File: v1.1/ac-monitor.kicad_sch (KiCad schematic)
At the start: 5 parts, among them U7 MID400

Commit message: cleanups all over
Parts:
- C10: renamed from C7; footprint Capacitor_SMD:C_0603_1608Metric_Pad1.05x0.95mm_HandSolder -> Capacitor_SMD:C_0603_1608Metric_Pad1.08x0.95mm_HandSolder
- R16: renamed from R29; footprint Resistor_SMD:R_1206_3216Metric_Pad1.42x1.75mm_HandSolder -> Resistor_SMD:R_1206_3216Metric_Pad1.30x1.75mm_HandSolder
- R17: renamed from R6; footprint Resistor_SMD:R_1206_3216Metric_Pad1.42x1.75mm_HandSolder -> Resistor_SMD:R_1206_3216Metric_Pad1.30x1.75mm_HandSolder
- R18: renamed from R30; footprint Resistor_SMD:R_0603_1608Metric_Pad1.05x0.95mm_HandSolder -> Resistor_SMD:R_0603_1608Metric_Pad0.98x0.95mm_HandSolder
- renumbered U7 to U5
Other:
- moved on the sheet: C10, R16, R17, R18, U5

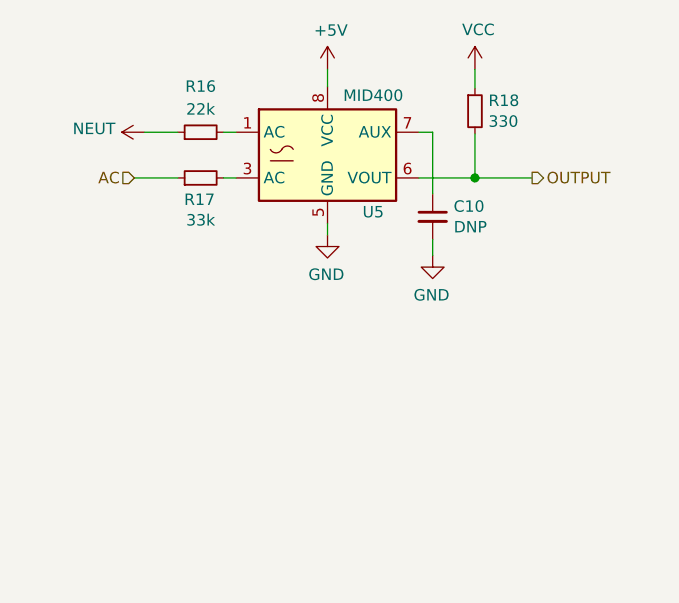
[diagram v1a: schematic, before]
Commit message: more work on smd triac routing
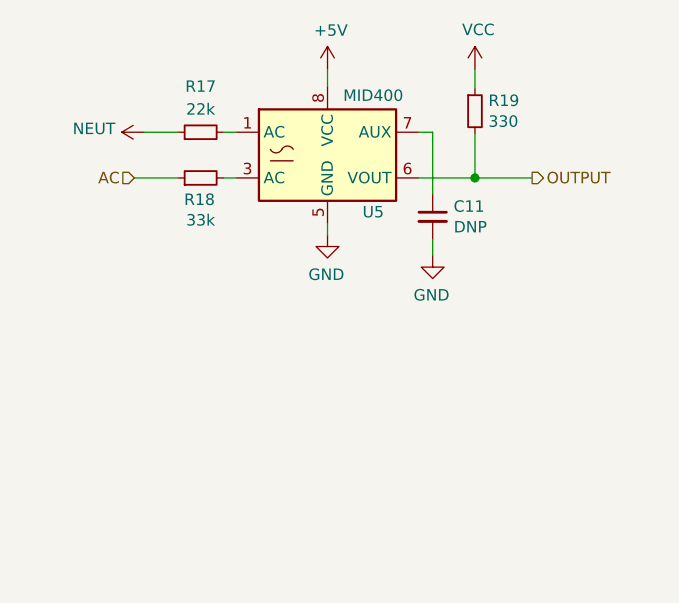
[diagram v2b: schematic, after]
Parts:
- renumbered C10 to C11, R16 to R17, R17 to R18, R18 to R19
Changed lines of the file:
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@@
   (symbol (lib_id "power:NEUT") (at 83.82 66.04 90)
     (in_bom yes) (on_board yes)
-    (property "Reference" "#PWR037" (id 0) (at 87.63 66.04 0)
+    (property "Reference" "#PWR040" (id 0) (at 87.63 66.04 0)
       (effects (font (size 1.27 1.27)) hide)
     )
@@
   (symbol (lib_id "power:+5V") (at 104.14 59.055 0)
     (in_bom yes) (on_board yes)
-    (property "Reference" "#PWR038" (id 0) (at 104.14 62.865 0)
+    (property "Reference" "#PWR041" (id 0) (at 104.14 62.865 0)
       (effects (font (size 1.27 1.27)) hide)
     )
@@
   (symbol (lib_id "power:VCC") (at 120.523 59.055 0)
     (in_bom yes) (on_board yes)
-    (property "Reference" "#PWR041" (id 0) (at 120.523 62.865 0)
+    (property "Reference" "#PWR044" (id 0) (at 120.523 62.865 0)
       (effects (font (size 1.27 1.27)) hide)
     )
@@
   (symbol (lib_id "power:GND") (at 104.14 77.47 0) (mirror y)
     (in_bom yes) (on_board yes)
-    (property "Reference" "#PWR039" (id 0) (at 104.14 83.82 0)
+    (property "Reference" "#PWR042" (id 0) (at 104.14 83.82 0)
       (effects (font (size 1.27 1.27)) hide)
     )
@@
   (symbol (lib_id "power:GND") (at 115.824 79.756 0) (mirror y)
     (in_bom yes) (on_board yes)
-    (property "Reference" "#PWR040" (id 0) (at 115.824 86.106 0)
+    (property "Reference" "#PWR043" (id 0) (at 115.824 86.106 0)
       (effects (font (size 1.27 1.27)) hide)
     )
@@
   (symbol (lib_id "Device:R_Small") (at 90.043 66.04 90)
     (in_bom yes) (on_board yes)
-    (property "Reference" "R16" (id 0) (at 90.043 60.96 90))
+    (property "Reference" "R17" (id 0) (at 90.043 60.96 90))
     (property "Value" "22k" (id 1) (at 90.043 63.5 90))
     (property "Footprint" "Resistor_SMD:R_1206_3216Metric_Pad1.30x1.75mm_HandSolder" (id 2) (at 90.043 66.04 0)
@@
   (symbol (lib_id "Device:R_Small") (at 90.043 71.12 90)
     (in_bom yes) (on_board yes)
-    (property "Reference" "R17" (id 0) (at 89.916 73.533 90))
+    (property "Reference" "R18" (id 0) (at 89.916 73.533 90))
     (property "Value" "33k" (id 1) (at 90.043 75.819 90))
     (property "Footprint" "Resistor_SMD:R_1206_3216Metric_Pad1.30x1.75mm_HandSolder" (id 2) (at 90.043 71.12 0)
@@
   (symbol (lib_id "Device:R_Small") (at 120.523 63.7032 0)
     (in_bom yes) (on_board yes)
-    (property "Reference" "R18" (id 0) (at 122.0216 62.5348 0)
+    (property "Reference" "R19" (id 0) (at 122.0216 62.5348 0)
       (effects (font (size 1.27 1.27)) (justify left))
     )
@@
   (symbol (lib_id "Device:C_Small") (at 115.824 75.438 0)
     (in_bom yes) (on_board yes)
-    (property "Reference" "C10" (id 0) (at 118.1482 74.2886 0)
+    (property "Reference" "C11" (id 0) (at 118.1482 74.2886 0)
       (effects (font (size 1.27 1.27)) (justify left))
     )

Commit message: more routing
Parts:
- R14: renamed from R17; value 22k -> 22k/0.5W
- R15: renamed from R18; value 33k -> 33k/0.5W
- renumbered C11 to C10, R19 to R16, U5 to U4
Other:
- title: (none) -> MadPresso controller
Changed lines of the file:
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@@
   (page 0 6)
   (paper "A5")
+  (title_block
+    (title "MadPresso controller")
+    (date "2020-11-18")
+    (rev "1.1")
+  )
   (junction (at 120.523 71.12) (diameter 1.016) (color 0 0 0 0))
   (wire (pts (xy 82.677 71.12) (xy 87.503 71.12))
@@
   (symbol (lib_id "power:NEUT") (at 83.82 66.04 90)
     (in_bom yes) (on_board yes)
-    (property "Reference" "#PWR040" (id 0) (at 87.63 66.04 0)
+    (property "Reference" "#PWR035" (id 0) (at 87.63 66.04 0)
       (effects (font (size 1.27 1.27)) hide)
     )
@@
   (symbol (lib_id "power:+5V") (at 104.14 59.055 0)
     (in_bom yes) (on_board yes)
-    (property "Reference" "#PWR041" (id 0) (at 104.14 62.865 0)
+    (property "Reference" "#PWR036" (id 0) (at 104.14 62.865 0)
       (effects (font (size 1.27 1.27)) hide)
     )
@@
   (symbol (lib_id "power:VCC") (at 120.523 59.055 0)
     (in_bom yes) (on_board yes)
-    (property "Reference" "#PWR044" (id 0) (at 120.523 62.865 0)
+    (property "Reference" "#PWR039" (id 0) (at 120.523 62.865 0)
       (effects (font (size 1.27 1.27)) hide)
     )
@@
   (symbol (lib_id "power:GND") (at 104.14 77.47 0) (mirror y)
     (in_bom yes) (on_board yes)
-    (property "Reference" "#PWR042" (id 0) (at 104.14 83.82 0)
+    (property "Reference" "#PWR037" (id 0) (at 104.14 83.82 0)
       (effects (font (size 1.27 1.27)) hide)
     )
@@
   (symbol (lib_id "power:GND") (at 115.824 79.756 0) (mirror y)
     (in_bom yes) (on_board yes)
-    (property "Reference" "#PWR043" (id 0) (at 115.824 86.106 0)
+    (property "Reference" "#PWR038" (id 0) (at 115.824 86.106 0)
       (effects (font (size 1.27 1.27)) hide)
     )
@@
   (symbol (lib_id "Device:R_Small") (at 90.043 66.04 90)
     (in_bom yes) (on_board yes)
-    (property "Reference" "R17" (id 0) (at 90.043 60.96 90))
-    (property "Value" "22k" (id 1) (at 90.043 63.5 90))
+    (property "Reference" "R14" (id 0) (at 90.043 60.96 90))
+    (property "Value" "22k/0.5W" (id 1) (at 90.043 63.5 90))
     (property "Footprint" "Resistor_SMD:R_1206_3216Metric_Pad1.30x1.75mm_HandSolder" (id 2) (at 90.043 66.04 0)
       (effects (font (size 1.27 1.27)) hide)
@@
   (symbol (lib_id "Device:R_Small") (at 90.043 71.12 90)
     (in_bom yes) (on_board yes)
-    (property "Reference" "R18" (id 0) (at 89.916 73.533 90))
-    (property "Value" "33k" (id 1) (at 90.043 75.819 90))
+    (property "Reference" "R15" (id 0) (at 89.916 73.533 90))
+    (property "Value" "33k/0.5W" (id 1) (at 90.043 75.819 90))
     (property "Footprint" "Resistor_SMD:R_1206_3216Metric_Pad1.30x1.75mm_HandSolder" (id 2) (at 90.043 71.12 0)
       (effects (font (size 1.27 1.27)) hide)
@@
   (symbol (lib_id "Device:R_Small") (at 120.523 63.7032 0)
     (in_bom yes) (on_board yes)
-    (property "Reference" "R19" (id 0) (at 122.0216 62.5348 0)
+    (property "Reference" "R16" (id 0) (at 122.0216 62.5348 0)
       (effects (font (size 1.27 1.27)) (justify left))
     )
@@
   (symbol (lib_id "Device:C_Small") (at 115.824 75.438 0)
     (in_bom yes) (on_board yes)
-    (property "Reference" "C11" (id 0) (at 118.1482 74.2886 0)
+    (property "Reference" "C10" (id 0) (at 118.1482 74.2886 0)
       (effects (font (size 1.27 1.27)) (justify left))
     )
@@
   (symbol (lib_id "Isolator:MID400") (at 104.14 68.58 0)
     (in_bom yes) (on_board yes)
-    (property "Reference" "U5" (id 0) (at 109.22 74.9108 0))
+    (property "Reference" "U4" (id 0) (at 109.22 74.9108 0))
     (property "Value" "MID400" (id 1) (at 109.22 61.9695 0))
     (property "Footprint" "Package_DIP:SMDIP-8_W7.62mm" (id 2) (at 104.14 68.58 0)

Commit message: v1.1a
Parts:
- renumbered C10 to C11, R14 to R17, R15 to R18, R16 to R19, U4 to U5
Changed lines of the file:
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@@
   (symbol (lib_id "power:NEUT") (at 83.82 66.04 90)
     (in_bom yes) (on_board yes)
-    (property "Reference" "#PWR035" (id 0) (at 87.63 66.04 0)
+    (property "Reference" "#PWR040" (id 0) (at 87.63 66.04 0)
       (effects (font (size 1.27 1.27)) hide)
     )
@@
   (symbol (lib_id "power:+5V") (at 104.14 59.055 0)
     (in_bom yes) (on_board yes)
-    (property "Reference" "#PWR036" (id 0) (at 104.14 62.865 0)
+    (property "Reference" "#PWR041" (id 0) (at 104.14 62.865 0)
       (effects (font (size 1.27 1.27)) hide)
     )
@@
   (symbol (lib_id "power:VCC") (at 120.523 59.055 0)
     (in_bom yes) (on_board yes)
-    (property "Reference" "#PWR039" (id 0) (at 120.523 62.865 0)
+    (property "Reference" "#PWR044" (id 0) (at 120.523 62.865 0)
       (effects (font (size 1.27 1.27)) hide)
     )
@@
   (symbol (lib_id "power:GND") (at 104.14 77.47 0) (mirror y)
     (in_bom yes) (on_board yes)
-    (property "Reference" "#PWR037" (id 0) (at 104.14 83.82 0)
+    (property "Reference" "#PWR042" (id 0) (at 104.14 83.82 0)
       (effects (font (size 1.27 1.27)) hide)
     )
@@
   (symbol (lib_id "power:GND") (at 115.824 79.756 0) (mirror y)
     (in_bom yes) (on_board yes)
-    (property "Reference" "#PWR038" (id 0) (at 115.824 86.106 0)
+    (property "Reference" "#PWR043" (id 0) (at 115.824 86.106 0)
       (effects (font (size 1.27 1.27)) hide)
     )
@@
   (symbol (lib_id "Device:R_Small") (at 90.043 66.04 90)
     (in_bom yes) (on_board yes)
-    (property "Reference" "R14" (id 0) (at 90.043 60.96 90))
+    (property "Reference" "R17" (id 0) (at 90.043 60.96 90))
     (property "Value" "22k/0.5W" (id 1) (at 90.043 63.5 90))
     (property "Footprint" "Resistor_SMD:R_1206_3216Metric_Pad1.30x1.75mm_HandSolder" (id 2) (at 90.043 66.04 0)
@@
   (symbol (lib_id "Device:R_Small") (at 90.043 71.12 90)
     (in_bom yes) (on_board yes)
-    (property "Reference" "R15" (id 0) (at 89.916 73.533 90))
+    (property "Reference" "R18" (id 0) (at 89.916 73.533 90))
     (property "Value" "33k/0.5W" (id 1) (at 90.043 75.819 90))
     (property "Footprint" "Resistor_SMD:R_1206_3216Metric_Pad1.30x1.75mm_HandSolder" (id 2) (at 90.043 71.12 0)
@@
   (symbol (lib_id "Device:R_Small") (at 120.523 63.7032 0)
     (in_bom yes) (on_board yes)
-    (property "Reference" "R16" (id 0) (at 122.0216 62.5348 0)
+    (property "Reference" "R19" (id 0) (at 122.0216 62.5348 0)
       (effects (font (size 1.27 1.27)) (justify left))
     )
@@
   (symbol (lib_id "Device:C_Small") (at 115.824 75.438 0)
     (in_bom yes) (on_board yes)
-    (property "Reference" "C10" (id 0) (at 118.1482 74.2886 0)
+    (property "Reference" "C11" (id 0) (at 118.1482 74.2886 0)
       (effects (font (size 1.27 1.27)) (justify left))
     )
@@
   (symbol (lib_id "Isolator:MID400") (at 104.14 68.58 0)
     (in_bom yes) (on_board yes)
-    (property "Reference" "U4" (id 0) (at 109.22 74.9108 0))
+    (property "Reference" "U5" (id 0) (at 109.22 74.9108 0))
     (property "Value" "MID400" (id 1) (at 109.22 61.9695 0))
     (property "Footprint" "Package_DIP:SMDIP-8_W7.62mm" (id 2) (at 104.14 68.58 0)
